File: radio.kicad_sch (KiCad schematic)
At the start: 28 parts, among them IC5 S2-LPQTR, IC6 BALF-SPI2-01D3, Y3 NX1612SA-50M-EXS00A-CS08403

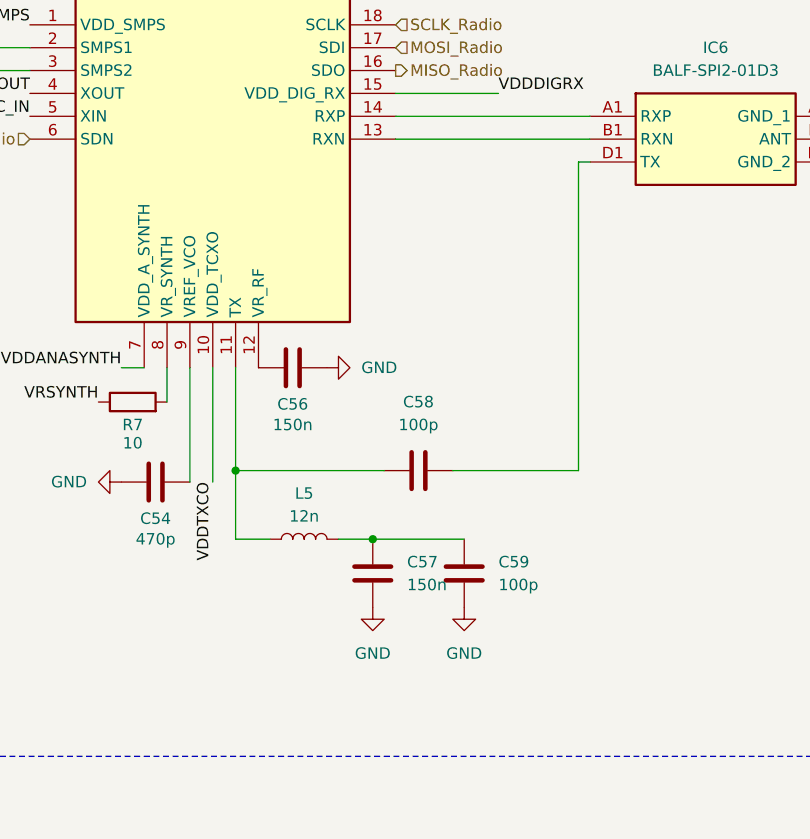
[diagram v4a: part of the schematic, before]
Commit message: Add footprints for inductors, missing one for L6
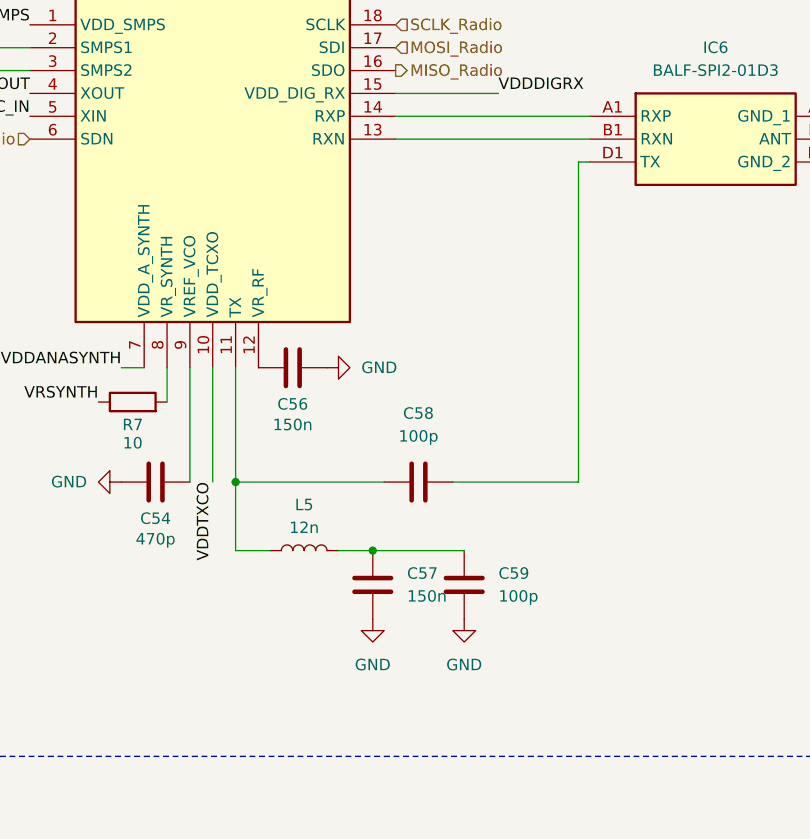
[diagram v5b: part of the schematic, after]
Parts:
- L2, L3: footprint (none) -> Inductor_SMD:L_0402_1005Metric_Pad0.77x0.64mm_HandSolder
- L4: footprint (none) -> Inductor_SMD:L_0805_2012Metric_Pad1.05x1.20mm_HandSolder
- L5: footprint (none) -> Inductor_SMD:L_0603_1608Metric_Pad1.05x0.95mm_HandSolder
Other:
- moved on the sheet: C57, C58, C59, L5
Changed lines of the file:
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@@
 	)
 	(junction
-		(at 171.45 124.46)
+		(at 110.49 77.47)
 		(diameter 0)
 		(color 0 0 0 0)
 	)
 	(junction
-		(at 110.49 77.47)
+		(at 261.62 87.63)
 		(diameter 0)
 		(color 0 0 0 0)
 	)
 	(junction
-		(at 261.62 87.63)
+		(at 120.65 77.47)
 		(diameter 0)
 		(color 0 0 0 0)
 	)
 	(junction
-		(at 120.65 77.47)
+		(at 171.45 125.73)
 		(diameter 0)
 		(color 0 0 0 0)
 	)
 	(junction
-		(at 186.69 132.08)
+		(at 186.69 133.35)
 		(diameter 0)
 		(color 0 0 0 0)
@@
 	(wire
 		(pts
-			(xy 171.45 124.46) (xy 187.96 124.46)
+			(xy 171.45 113.03) (xy 171.45 125.73)
 		)
 		(stroke
@@
 	(wire
 		(pts
-			(xy 168.91 125.73) (xy 168.91 113.03)
+			(xy 171.45 125.73) (xy 187.96 125.73)
 		)
 		(stroke
@@
 	(wire
 		(pts
-			(xy 71.12 39.37) (xy 74.93 39.37)
+			(xy 168.91 125.73) (xy 168.91 113.03)
 		)
 		(stroke
@@
 	(wire
 		(pts
-			(xy 74.93 113.03) (xy 85.09 113.03)
+			(xy 71.12 39.37) (xy 74.93 39.37)
 		)
 		(stroke
@@
 	(wire
 		(pts
-			(xy 209.55 124.46) (xy 209.55 90.17)
+			(xy 74.93 113.03) (xy 85.09 113.03)
 		)
 		(stroke
@@
 	(wire
 		(pts
-			(xy 171.45 124.46) (xy 171.45 132.08)
+			(xy 209.55 125.73) (xy 209.55 90.17)
 		)
 		(stroke
@@
 	(wire
 		(pts
-			(xy 182.88 132.08) (xy 186.69 132.08)
+			(xy 182.88 133.35) (xy 186.69 133.35)
 		)
 		(stroke
@@
 	(wire
 		(pts
-			(xy 171.45 113.03) (xy 171.45 124.46)
+			(xy 129.54 77.47) (xy 132.08 77.47)
 		)
 		(stroke
@@
 	(wire
 		(pts
-			(xy 129.54 77.47) (xy 132.08 77.47)
+			(xy 238.76 87.63) (xy 248.92 87.63)
 		)
 		(stroke
@@
 	(wire
 		(pts
-			(xy 238.76 87.63) (xy 248.92 87.63)
+			(xy 171.45 133.35) (xy 175.26 133.35)
 		)
 		(stroke
@@
 	(wire
 		(pts
-			(xy 171.45 132.08) (xy 175.26 132.08)
+			(xy 195.58 125.73) (xy 209.55 125.73)
 		)
 		(stroke
@@
 	(wire
 		(pts
-			(xy 195.58 124.46) (xy 209.55 124.46)
+			(xy 171.45 125.73) (xy 171.45 133.35)
 		)
 		(stroke
@@
 	(wire
 		(pts
-			(xy 186.69 132.08) (xy 196.85 132.08)
+			(xy 186.69 133.35) (xy 196.85 133.35)
 		)
 		(stroke
@@
 	(symbol
 		(lib_id "Device:C")
-		(at 191.77 124.46 90)
+		(at 191.77 125.73 90)
 		(unit 1)
 		(exclude_from_sim no)
@@
 		(fields_autoplaced yes)
 		(property "Reference" "C58"
-			(at 191.77 116.84 90)
+			(at 191.77 118.11 90)
 			(effects
 				(font
@@
 		)
 		(property "Value" "100p"
-			(at 191.77 119.38 90)
+			(at 191.77 120.65 90)
 			(effects
 				(font
@@
 		)
 		(property "Footprint" "Capacitor_SMD:C_0603_1608Metric_Pad1.08x0.95mm_HandSolder"
-			(at 195.58 123.4948 0)
+			(at 195.58 124.7648 0)
 			(effects
 				(font
@@
 		)
 		(property "Datasheet" "~"
-			(at 191.77 124.46 0)
+			(at 191.77 125.73 0)
 			(effects
 				(font
@@
 		)
 		(property "Description" "Unpolarized capacitor"
-			(at 191.77 124.46 0)
+			(at 191.77 125.73 0)
 			(effects
 				(font
@@
 			)
 		)
-		(property "Footprint" ""
+		(property "Footprint" "Inductor_SMD:L_0402_1005Metric_Pad0.77x0.64mm_HandSolder"
 			(at 125.73 77.47 0)
 			(effects
@@
 			)
 		)
-		(property "Datasheet" "~"
+		(property "Datasheet" "https://www.mouser.fr/datasheet/3/76/2/JELF243B_0010.pdf"
 			(at 125.73 77.47 0)
 			(effects
@@
 	(symbol
 		(lib_id "power:GND")
-		(at 196.85 139.7 0)
+		(at 196.85 140.97 0)
 		(unit 1)
 		(exclude_from_sim no)
@@
 		(fields_autoplaced yes)
 		(property "Reference" "#PWR089"
-			(at 196.85 146.05 0)
+			(at 196.85 147.32 0)
 			(effects
 				(font
@@
 		)
 		(property "Value" "GND"
-			(at 196.85 144.78 0)
+			(at 196.85 146.05 0)
 			(effects
 				(font
@@
 		)
 		(property "Footprint" ""
-			(at 196.85 139.7 0)
+			(at 196.85 140.97 0)
 			(effects
 				(font
@@
 		)
 		(property "Datasheet" ""
-			(at 196.85 139.7 0)
+			(at 196.85 140.97 0)
 			(effects
 				(font
@@
 		)
 		(property "Description" "Power symbol creates a global label with name \"GND\" , ground"
-			(at 196.85 139.7 0)
+			(at 196.85 140.97 0)
 			(effects
 				(font
@@
 			)
 		)
-		(property "Footprint" ""
+		(property "Footprint" "Inductor_SMD:L_0402_1005Metric_Pad0.77x0.64mm_HandSolder"
 			(at 58.42 153.67 0)
 			(effects
@@
 			)
 		)
-		(property "Datasheet" "~"
+		(property "Datasheet" "https://www.mouser.fr/datasheet/3/1017/1/jti_cat_rf_ind_HP0cWdS.pdf"
 			(at 58.42 153.67 0)
 			(effects
@@
 	(symbol
 		(lib_id "Device:C")
-		(at 186.69 135.89 0)
+		(at 186.69 137.16 0)
 		(unit 1)
 		(exclude_from_sim no)
@@
 		(fields_autoplaced yes)
 		(property "Reference" "C57"
-			(at 190.5 134.6199 0)
+			(at 190.5 135.8899 0)
 			(effects
 				(font
@@
 		)
 		(property "Value" "150n"
-			(at 190.5 137.1599 0)
+			(at 190.5 138.4299 0)
 			(effects
 				(font
@@
 		)
 		(property "Footprint" "Capacitor_SMD:C_0603_1608Metric_Pad1.08x0.95mm_HandSolder"
-			(at 187.6552 139.7 0)
+			(at 187.6552 140.97 0)
 			(effects
 				(font
@@
 		)
 		(property "Datasheet" "~"
-			(at 186.69 135.89 0)
+			(at 186.69 137.16 0)
 			(effects
 				(font
@@
 		)
 		(property "Description" "Unpolarized capacitor"
-			(at 186.69 135.89 0)
+			(at 186.69 137.16 0)
 			(effects
 				(font
@@
 	(symbol
 		(lib_id "Device:L")
-		(at 179.07 132.08 90)
+		(at 179.07 133.35 90)
 		(unit 1)
 		(exclude_from_sim no)
@@
 		(fields_autoplaced yes)
 		(property "Reference" "L5"
-			(at 179.07 127 90)
+			(at 179.07 128.27 90)
 			(effects
 				(font
@@
 		)
 		(property "Value" "12n"
-			(at 179.07 129.54 90)
+			(at 179.07 130.81 90)
 			(effects
 				(font
@@
 			)
 		)
-		(property "Footprint" ""
-			(at 179.07 132.08 0)
+		(property "Footprint" "Inductor_SMD:L_0603_1608Metric_Pad1.05x0.95mm_HandSolder"
+			(at 179.07 133.35 0)
 			(effects
 				(font
@@
 			)
 		)
-		(property "Datasheet" "~"
-			(at 179.07 132.08 0)
+		(property "Datasheet" "https://www.mouser.fr/datasheet/3/76/2/JELF243A_0024.pdf"
+			(at 179.07 133.35 0)
 			(effects
 				(font
@@
 		)
 		(property "Description" "Inductor"
-			(at 179.07 132.08 0)
+			(at 179.07 133.35 0)
 			(effects
 				(font
@@
 	(symbol
 		(lib_id "power:GND")
-		(at 186.69 139.7 0)
+		(at 186.69 140.97 0)
 		(unit 1)
 		(exclude_from_sim no)
@@
 		(fields_autoplaced yes)
 		(property "Reference" "#PWR088"
-			(at 186.69 146.05 0)
+			(at 186.69 147.32 0)
 			(effects
 				(font
@@
 		)
 		(property "Value" "GND"
-			(at 186.69 144.78 0)
+			(at 186.69 146.05 0)
 			(effects
 				(font
@@
 		)
 		(property "Footprint" ""
-			(at 186.69 139.7 0)
+			(at 186.69 140.97 0)
 			(effects
 				(font
@@
 		)
 		(property "Datasheet" ""
-			(at 186.69 139.7 0)
+			(at 186.69 140.97 0)
 			(effects
 				(font
@@
 		)
 		(property "Description" "Power symbol creates a global label with name \"GND\" , ground"
-			(at 186.69 139.7 0)
+			(at 186.69 140.97 0)
 			(effects
 				(font
@@
 	(symbol
 		(lib_id "Device:C")
-		(at 196.85 135.89 180)
+		(at 196.85 137.16 180)
 		(unit 1)
 		(exclude_from_sim no)
@@
 		(fields_autoplaced yes)
 		(property "Reference" "C59"
-			(at 200.66 134.6199 0)
+			(at 200.66 135.8899 0)
 			(effects
 				(font
@@
 		)
 		(property "Value" "100p"
-			(at 200.66 137.1599 0)
+			(at 200.66 138.4299 0)
 			(effects
 				(font
@@
 		)
 		(property "Footprint" "Capacitor_SMD:C_0603_1608Metric_Pad1.08x0.95mm_HandSolder"
-			(at 195.8848 132.08 0)
+			(at 195.8848 133.35 0)
 			(effects
 				(font
@@
 		)
 		(property "Datasheet" "~"
-			(at 196.85 135.89 0)
+			(at 196.85 137.16 0)
 			(effects
 				(font
@@
 		)
 		(property "Description" "Unpolarized capacitor"
-			(at 196.85 135.89 0)
+			(at 196.85 137.16 0)
 			(effects
 				(font
@@
 			)
 		)
-		(property "Footprint" ""
+		(property "Footprint" "Inductor_SMD:L_0805_2012Metric_Pad1.05x1.20mm_HandSolder"
 			(at 135.89 77.47 0)
 			(effects
@@
 			)
 		)
-		(property "Datasheet" "~"
+		(property "Datasheet" "https://www.mouser.fr/datasheet/3/76/2/JELF243B_0011.pdf"
 			(at 135.89 77.47 0)
 			(effects

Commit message: Components reindexing and update of PCB
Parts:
- renumbered C44 to C43, C55 to C44, C52 to C46, C53 to C47, C46 to C48, C60 to C49, C61 to C50, C47 to C51, C50 to C52, C56 to C53, C48 to C54, C51 to C55, C54 to C56, C58 to C57, C57 to C58, C43 to C60, C49 to C61, L3 to L2, L4 to L3, L5 to L4, L2 to L5

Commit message: Place MCU and its components around
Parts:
- renumbered C43 to C42, C44 to C43, C45 to C44, C46 to C45, C47 to C46, C48 to C47, C49 to C48, C50 to C49, C51 to C50, C52 to C51, C53 to C52, C54 to C53, C55 to C54, C56 to C55, C57 to C56, C58 to C57, C59 to C58, C60 to C59, C61 to C60

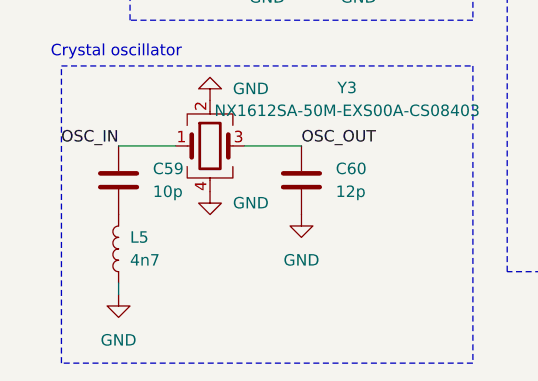
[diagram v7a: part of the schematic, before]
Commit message: Remove L5 inductos on radio oscillator
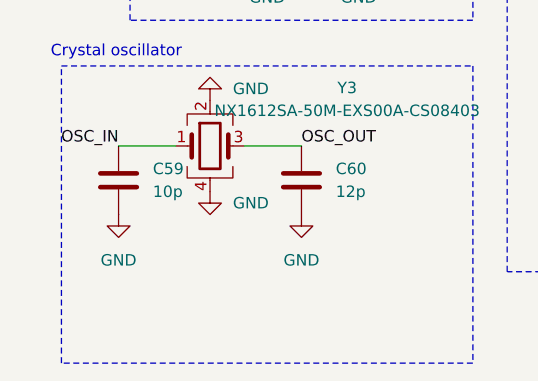
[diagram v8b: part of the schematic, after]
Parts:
- removed L5: 4n7, Inductor_SMD:L_0402_1005Metric_Pad0.77x0.64mm_HandSolder, symbol Device:L
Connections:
- net GND: now also C59.2
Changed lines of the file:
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@@
 	(wire
 		(pts
-			(xy 58.42 158.75) (xy 58.42 157.48)
-		)
-		(stroke
-			(width 0)
-			(type default)
-		)
-	)
-	(wire
-		(pts
 			(xy 158.75 113.03) (xy 161.29 113.03)
 		)
@@
 	)
 	(symbol
-		(lib_id "Device:L")
-		(at 58.42 153.67 180)
-		(unit 1)
-		(exclude_from_sim no)
-		(in_bom yes)
-		(on_board yes)
-		(dnp no)
-		(fields_autoplaced yes)
-		(property "Reference" "L5"
-			(at 59.69 152.3999 0)
-			(effects
-				(font
-					(size 1.27 1.27)
-				)
-				(justify right)
-			)
-		)
-		(property "Value" "4n7"
-			(at 59.69 154.9399 0)
-			(effects
-				(font
-					(size 1.27 1.27)
-				)
-				(justify right)
-			)
-		)
-		(property "Footprint" "Inductor_SMD:L_0402_1005Metric_Pad0.77x0.64mm_HandSolder"
-			(at 58.42 153.67 0)
-			(effects
-				(font
-					(size 1.27 1.27)
-				)
-				(hide yes)
-			)
-		)
-		(property "Datasheet" "https://www.mouser.fr/datasheet/3/1017/1/jti_cat_rf_ind_HP0cWdS.pdf"
-			(at 58.42 153.67 0)
-			(effects
-				(font
-					(size 1.27 1.27)
-				)
-				(hide yes)
-			)
-		)
-		(property "Description" "Inductor"
-			(at 58.42 153.67 0)
-			(effects
-				(font
-					(size 1.27 1.27)
-				)
-				(hide yes)
-			)
-		)
-		(pin "2"
-		)
-		(pin "1"
-		)
-		(instances
-			(project "weather-station-poc"
-				(path "/38eb53bb-294e-46e4-ad59-fd355ca373b9/31741ecc-719f-4191-b75e-d75152dfd251"
-					(reference "L5")
-					(unit 1)
-				)
-			)
-		)
-	)
-	(symbol
 		(lib_id "Device:C")
 		(at 162.56 125.73 90)
@@
 		(dnp no)
 		(fields_autoplaced yes)
-		(property "Reference" "#PWR090"
+		(property "Reference" "#PWR091"
 			(at 78.74 156.21 0)
 			(effects
@@
 			(project "weather-station-poc"
 				(path "/38eb53bb-294e-46e4-ad59-fd355ca373b9/31741ecc-719f-4191-b75e-d75152dfd251"
-					(reference "#PWR090")
+					(reference "#PWR091")
 					(unit 1)
 				)
@@
 	(symbol
 		(lib_id "power:GND")
-		(at 58.42 158.75 0)
+		(at 58.42 149.86 0)
 		(unit 1)
 		(exclude_from_sim no)
@@
 		(dnp no)
 		(fields_autoplaced yes)
-		(property "Reference" "#PWR091"
-			(at 58.42 165.1 0)
+		(property "Reference" "#PWR090"
+			(at 58.42 156.21 0)
 			(effects
 				(font
@@
 		)
 		(property "Value" "GND"
-			(at 58.42 163.83 0)
+			(at 58.42 154.94 0)
 			(effects
 				(font
@@
 		)
 		(property "Footprint" ""
-			(at 58.42 158.75 0)
+			(at 58.42 149.86 0)
 			(effects
 				(font
@@
 		)
 		(property "Datasheet" ""
-			(at 58.42 158.75 0)
+			(at 58.42 149.86 0)
 			(effects
 				(font
@@
 		)
 		(property "Description" "Power symbol creates a global label with name \"GND\" , ground"
-			(at 58.42 158.75 0)
+			(at 58.42 149.86 0)
 			(effects
 				(font
@@
 			(project "weather-station-poc"
 				(path "/38eb53bb-294e-46e4-ad59-fd355ca373b9/31741ecc-719f-4191-b75e-d75152dfd251"
-					(reference "#PWR091")
+					(reference "#PWR090")
 					(unit 1)
 				)
